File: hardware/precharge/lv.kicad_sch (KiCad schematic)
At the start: 44 parts

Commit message: Tweaks made during today's meeting
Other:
- note added: "Add a tiny delay from when SHUTDOWN changes, to prevent a glitch on FAULT due to unknown initial state of flip-flop."
- note removed: "Add a tiny delay from when SHUTDOWN changes, to prevent a glitch on FAULT."
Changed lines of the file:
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@@
     (effects (font (size 1.27 1.27)) (justify left bottom))
   )
-  (text "Add a tiny delay from\nwhen SHUTDOWN changes,\nto prevent a glitch on\nFAULT."
-    (at 155.575 123.825 0)
+  (text "Add a tiny delay from\nwhen SHUTDOWN changes,\nto prevent a glitch on\nFAULT due to unknown\ninitial state of\nflip-flop."
+    (at 131.445 133.35 0)
     (effects (font (size 1.27 1.27)) (justify left bottom))
   )

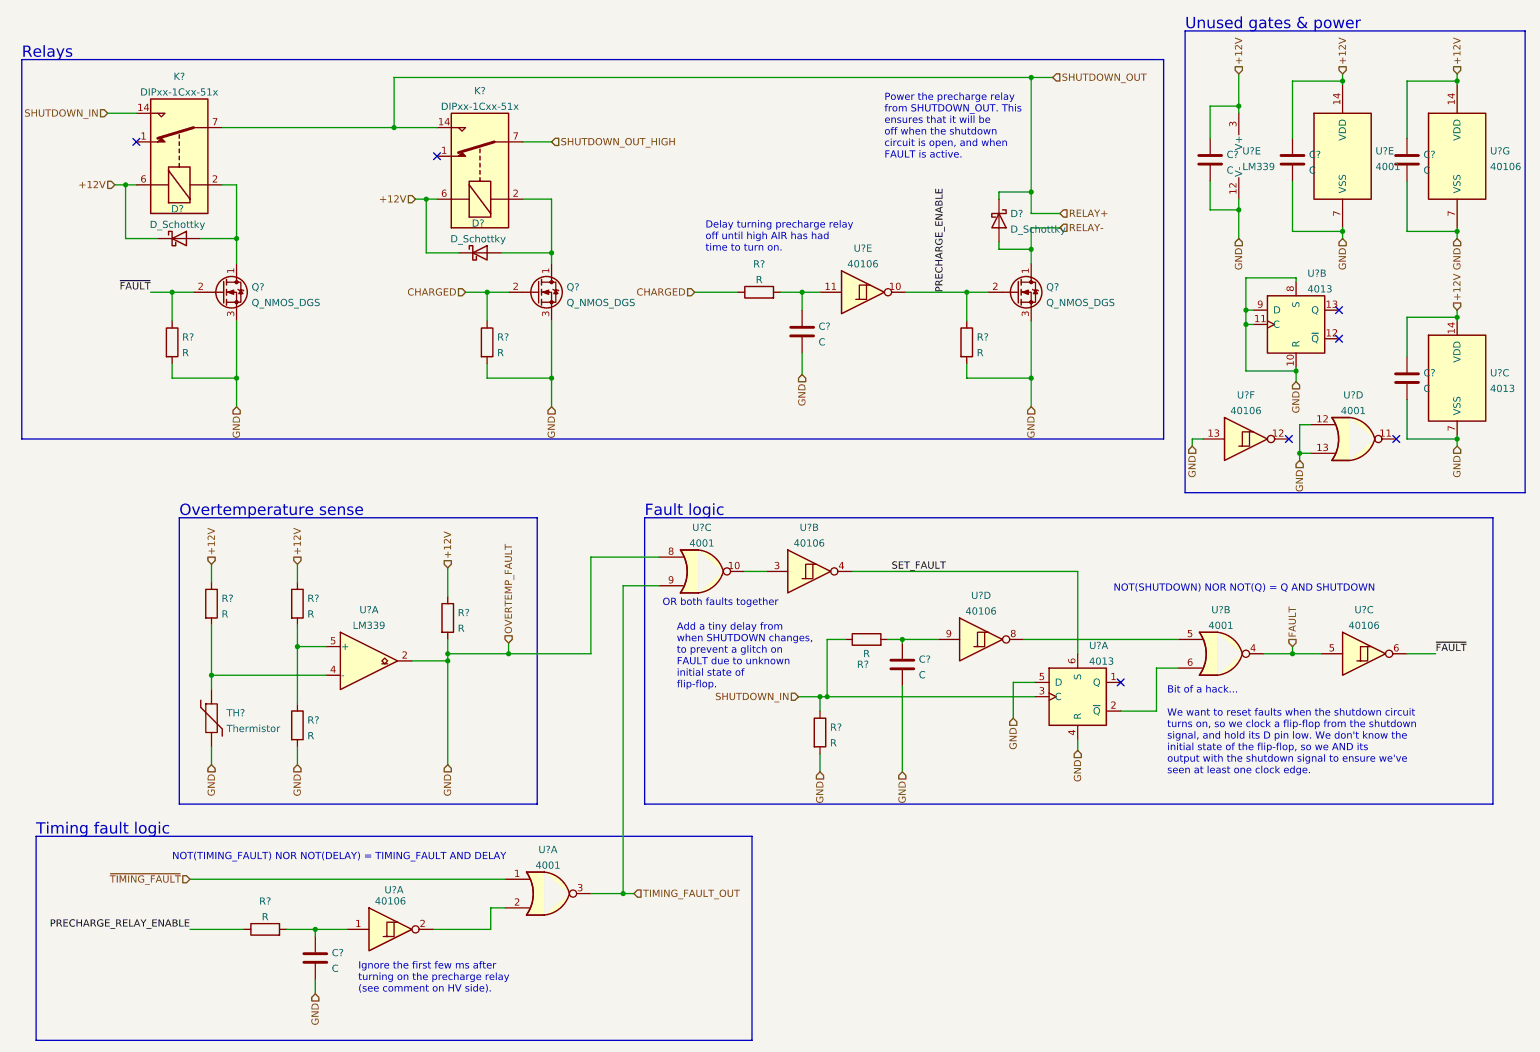
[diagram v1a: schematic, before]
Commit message: Updated quite a bit
- Added relay mechanical state detection

- Selected most component values for HV side

- Other miscellaneous changes
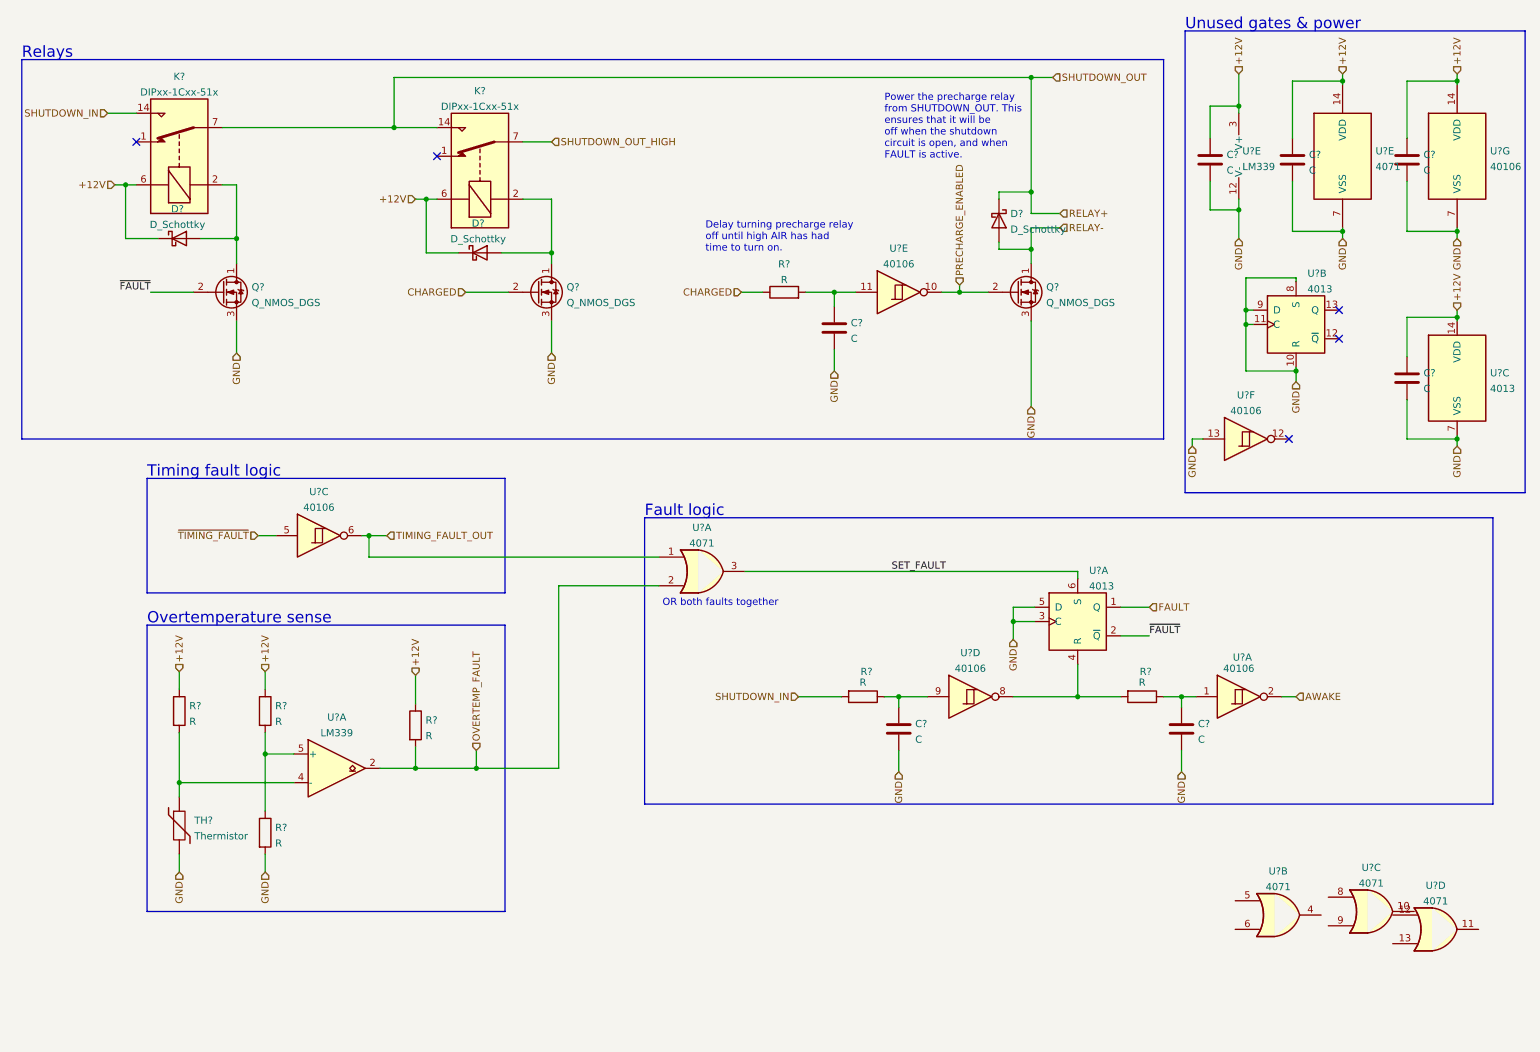
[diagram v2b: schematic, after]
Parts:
- removed C?: C, symbol Device:C
- removed R? (x5): R, symbol Device:R
- removed U? (x5): 4001, symbol 4xxx:4001
- removed U? (x2): 40106, symbol 4xxx:40106
- added C?: C, symbol Device:C
- added R?: R, symbol Device:R
- added U?: 40106, symbol 4xxx:40106
- added U? (x5): 4071, symbol 4xxx:4071
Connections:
- net +12V: now also U?.14 (VDD)
- net FAULT: now also U?.1 (Q); no longer U?.5
- net GND: now also C?.1, U?.3 (C), C?.1, U?.7 (VSS); no longer C?.2, R?.2, U?.2, U?.4 (R)
- net SET_FAULT: now also U?.3
- net SHUTDOWN_IN: now also R?.2; no longer R?.1, U?.3 (C)
- net TIMING_FAULT_OUT: now also U?.6, U?.1
- net ~{FAULT}: now also U?.2 (~{Q}); no longer U?.6
- net ~{TIMING_FAULT}: now also U?.5
- net at U?.1: now also C?.2, R?.1
- net AWAKE: now reaches U?.2
- net PRECHARGE_ENABLE renamed PRECHARGE_ENABLED
- new net: R?.2, U?.4 (R), U?.8
- new net: C?.2, R?.1, U?.9
- new net OVERTEMP_FAULT: R?.2, U?.2, U?.2
- no-connect marks 7 -> 5
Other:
- note removed: "Add a tiny delay from when SHUTDOWN changes, to prevent a glitch on FAULT due to unknown initial state of flip-flop."
- note removed: "Bit of a hack... We want to reset faults when the shutdown circuit turns on, so we clock a flip-flop from the shutdown signal, and hold its D pin low. We don't know the initial state of the flip-flop, so we AND its output with the shutdown signal to ensure we've seen at least one clock edge."
- note removed: "Ignore the first few ms after turning on the precharge relay (see comment on HV side)."
- note removed: "NOT(SHUTDOWN) NOR NOT(Q) = Q AND SHUTDOWN"
- note removed: "NOT(TIMING_FAULT) NOR NOT(DELAY) = TIMING_FAULT AND DELAY"
- moved on the sheet: C?, R?, TH?, U?A, U?C, U?E

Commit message: Added part numbers for most components, added LEDs, tweaked LV side.
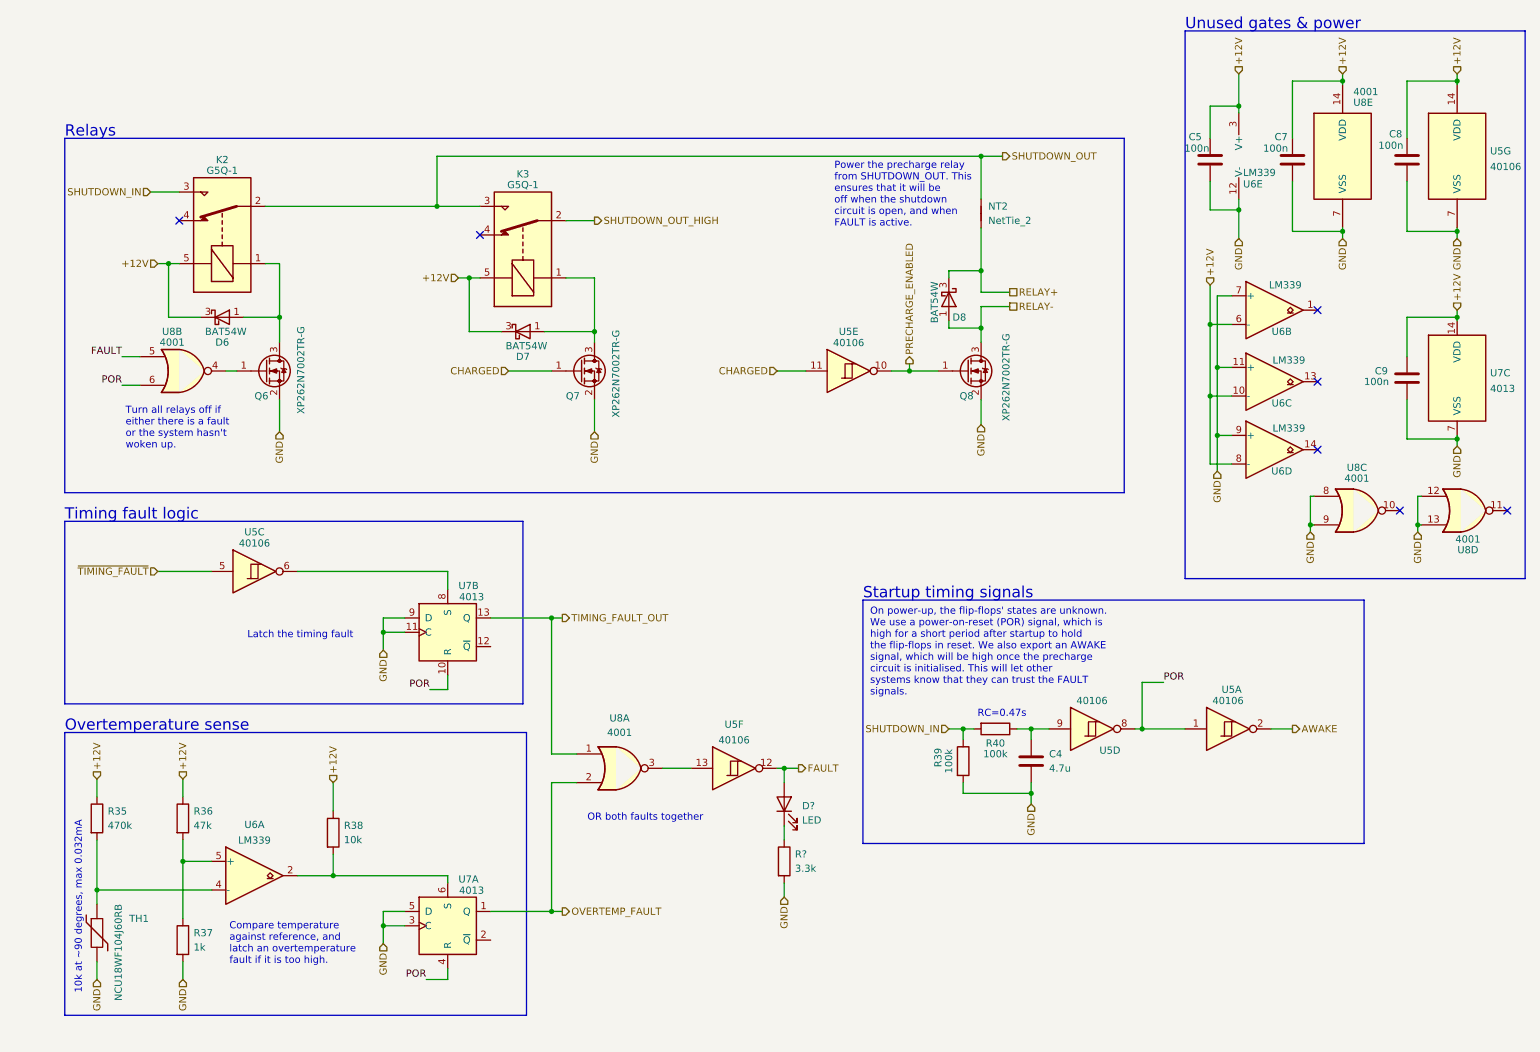
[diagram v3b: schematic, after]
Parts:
- removed C? (x2): C, symbol Device:C
- removed D? (x3): D_Schottky, symbol Device:D_Schottky
- removed K? (x2): DIPxx-1Cxx-51x, Relay_THT:Relay_StandexMeder_DIP_LowProfile, symbol Relay:DIPxx-1Cxx-51x
- removed Q? (x3): Q_NMOS_DGS, symbol Device:Q_NMOS_DGS
- removed R? (x2): R, symbol Device:R
- removed U? (x5): 4071, symbol 4xxx:4071
- added D6, D7, D8: BAT54W, Package_TO_SOT_SMD:SOT-323_SC-70, symbol Diode:BAT54W
- added D?: LED, symbol Device:LED
- added K2, K3: G5Q-1, Relay_THT:Relay_SPDT_Omron-G5Q-1, symbol Relay:G5Q-1
- added NT2: NetTie_2, symbol Device:NetTie_2
- added Q6, Q7, Q8: XP262N7002TR-G, symbol Device:Q_NMOS_GSD
- added R39: 100k, symbol Device:R
- added R?: 3.3k, symbol Device:R
- added unit 2 of U6
- added unit 4 of U6
- added unit 3 of U6
- added U8: 4001, symbol 4xxx:4001
- C4: renamed from C?; value C -> 4.7u
- C5, C7, C8, C9: renamed from C?; value C -> 100n
- R35: renamed from R?; value R -> 470k
- R36: renamed from R?; value R -> 47k
- R37: renamed from R?; value R -> 1k
- R38: renamed from R?; value R -> 10k
- R40: renamed from R?; value R -> 100k
- TH1: renamed from TH?; value Thermistor -> NCU18WF104J60RB
- gave numbers to parts that had none: 3
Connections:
- net +12V: now also D6.3 (K), D7.3 (K), K2.5, K3.5, U6.10 (-), U6.6 (-), U6.8 (-), U8.14 (VDD)
- net CHARGED: now also U5.11, Q7.1 (G)
- net FAULT: now also U5.12, D?.2 (A), U8.5; no longer U7.1 (Q)
- net GND: now also Q6.2 (S), Q7.2 (S), Q8.2 (S), R39.2, R?.2, U6.11 (+), U6.7 (+), U6.9 (+), U8.12, U8.13, U8.7 (VSS), U8.8, U8.9; no longer U5.13, U7.10 (R), U7.8 (S)
- net OVERTEMP_FAULT: now also U7.1 (Q), U8.2; no longer R38.2, U6.2
- net PRECHARGE_ENABLED: now also Q8.1 (G)
- net RELAY+: now also D8.3 (K), NT2.1
- net RELAY-: now also D8.1 (A), Q8.3 (D)
- net SHUTDOWN_IN: now also K2.3, R39.1
- net SHUTDOWN_OUT_HIGH: now also K3.2
- net TIMING_FAULT_OUT: now also U7.13 (Q), U8.1; no longer U5.6
- net POR: now reaches U5.8, U7.4 (R)
- net POR: now also U5.1, U7.10 (R), U8.6
- net SET_FAULT: no longer names the net of U7.6 (S)
- net SET_FAULT: now also R38.2, U6.2
- net ~{FAULT}: no longer names the net of U7.2 (~{Q})
- new net: Q6.1 (G), U8.4
- new net: D6.1 (A), K2.1, Q6.3 (D)
- new net: D?.1 (K), R?.1
- new net: D7.1 (A), K3.1, Q7.3 (D)
- new net: U5.13, U8.3
- new net: U5.6, U7.8 (S)
- new net SHUTDOWN_OUT: K2.2, K3.3, NT2.2
- no-connect marks 5 -> 7
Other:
- note added: "10k at ~90 degrees, max 0.032mA"
- note added: "Compare temperature against reference, and latch an overtemperature fault if it is too high."
- note added: "Latch the timing fault"
- note added: "On power-up, the flip-flops' states are unknown. We use a power-on-reset (POR) signal, which is high for a short period after startup to hold the flip-flops in reset. We also export an AWAKE signal, which will be high once the precharge circuit is initialised. This will let other systems know that they can trust the FAULT signals."
- note added: "RC=0.47s"
- note added: "Startup timing signals"
- note added: "Turn all relays off if either there is a fault or the system hasn't woken up."
- note removed: "Delay turning precharge relay off until high AIR has had time to turn on."
- note removed: "Fault logic"
- moved on the sheet: C4, R35, R36, R37, R38, R40, TH1, U5A, U5C, U5D, U5E, U5F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

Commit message: Tweaks, nearly done
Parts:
- gave numbers to parts that had none: 2
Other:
- moved on the sheet: U5F
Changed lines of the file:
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@@
     (stroke (width 0) (type default) (color 0 0 0 0))
   )
-  (wire (pts (xy 128.905 147.32) (xy 133.985 147.32))
+  (wire (pts (xy 128.905 147.32) (xy 130.175 147.32))
     (stroke (width 0) (type default) (color 0 0 0 0))
   )
@@
     (stroke (width 0) (type default) (color 0 0 0 0))
   )
-  (wire (pts (xy 149.225 147.32) (xy 150.495 147.32))
+  (wire (pts (xy 145.415 147.32) (xy 150.495 147.32))
     (stroke (width 0) (type default) (color 0 0 0 0))
   )
@@
   (symbol (lib_id "Device:R") (at 150.495 163.83 0) (unit 1)
     (in_bom yes) (on_board yes) (fields_autoplaced)
-    (property "Reference" "R?" (id 0) (at 152.4 162.5599 0)
+    (property "Reference" "R46" (id 0) (at 152.4 162.5599 0)
       (effects (font (size 1.27 1.27)) (justify left))
     )
@@
   (symbol (lib_id "Device:LED") (at 150.495 153.67 90) (unit 1)
     (in_bom yes) (on_board yes) (fields_autoplaced)
-    (property "Reference" "D?" (id 0) (at 153.67 153.9874 90)
+    (property "Reference" "D14" (id 0) (at 153.67 153.9874 90)
       (effects (font (size 1.27 1.27)) (justify right))
     )
@@
     (pin "2")
   )
-  (symbol (lib_id "4xxx:40106") (at 141.605 147.32 0) (unit 6)
+  (symbol (lib_id "4xxx:40106") (at 137.795 147.32 0) (unit 6)
     (in_bom yes) (on_board yes) (fields_autoplaced)
-    (property "Reference" "U5" (id 0) (at 141.605 139.5435 0))
-    (property "Value" "40106" (id 1) (at 141.605 142.3186 0))
-    (property "Footprint" "" (id 2) (at 141.605 147.32 0)
-      (effects (font (size 1.27 1.27)) hide)
-    )
-    (property "Datasheet" "https://assets.nexperia.com/documents/data-sheet/HEF40106B.pdf" (id 3) (at 141.605 147.32 0)
-      (effects (font (size 1.27 1.27)) hide)
-    )
+    (property "Reference" "U5" (id 0) (at 137.795 139.5435 0))
+    (property "Value" "40106" (id 1) (at 137.795 142.3186 0))
+    (property "Footprint" "" (id 2) (at 137.795 147.32 0)
+      (effects (font (size 1.27 1.27)) hide)
+    )
+    (property "Datasheet" "https://assets.nexperia.com/documents/data-sheet/HEF40106B.pdf" (id 3) (at 137.795 147.32 0)
+      (effects (font (size 1.27 1.27)) hide)
+    )

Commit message: Assigned some footprints, created footprint library
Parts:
- C4: footprint (none) -> Capacitor_SMD:C_0805_2012Metric
- C5, C7, C8, C9: footprint (none) -> Capacitor_SMD:C_0603_1608Metric
- D14: footprint (none) -> LED_SMD:LED_0603_1608Metric
- NT2: footprint (none) -> NetTie:NetTie-2_SMD_Pad0.5mm
- Q6, Q7, Q8: footprint (none) -> Package_TO_SOT_SMD:SOT-23
- R35, R36, R37, R38, R39, R40, R46, TH1: footprint (none) -> Resistor_SMD:R_0603_1608Metric
- U5, U6, U7, U8: footprint (none) -> Package_SO:SOIC-14_3.9x8.7mm_P1.27mm

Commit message: Preliminary PCB placement
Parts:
- removed C4: 4.7u, Capacitor_SMD:C_0805_2012Metric, symbol Device:C
- added C13: 4.7u, Capacitor_THT:CP_Radial_D5.0mm_P2.00mm, symbol Device:C_Polarized
- K2, K3: value G5Q-1 -> G5Q-1EU DC12
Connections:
- net GND: now also C13.2
- net at R40.1, U5.9: now also C13.1
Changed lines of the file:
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@@
     (in_bom yes) (on_board yes)
     (property "Reference" "K2" (id 0) (at 50.8 39.37 90))
-    (property "Value" "G5Q-1" (id 1) (at 50.8 41.275 90))
+    (property "Value" "G5Q-1EU DC12" (id 1) (at 50.8 41.275 90))
     (property "Footprint" "Relay_THT:Relay_SPDT_Omron-G5Q-1" (id 2) (at 52.07 41.275 0)
       (effects (font (size 1.27 1.27)) (justify left) hide)
@@
     (pin "9")
   )
-  (symbol (lib_id "Device:C") (at 194.31 146.05 180) (unit 1)
-    (in_bom yes) (on_board yes)
-    (property "Reference" "C4" (id 0) (at 197.485 144.78 0)
-      (effects (font (size 1.27 1.27)) (justify right))
-    )
-    (property "Value" "4.7u" (id 1) (at 197.485 147.32 0)
-      (effects (font (size 1.27 1.27)) (justify right))
-    )
-    (property "Footprint" "Capacitor_SMD:C_0805_2012Metric" (id 2) (at 193.3448 142.24 0)
-      (effects (font (size 1.27 1.27)) hide)
-    )
-    (property "Datasheet" "~" (id 3) (at 194.31 146.05 0)
-      (effects (font (size 1.27 1.27)) hide)
-    )
-    (pin "1")
-    (pin "2")
-  )
   (symbol (lib_id "Comparator:LM339") (at 233.68 38.735 0) (unit 5)
     (in_bom yes) (on_board yes)
@@
     (in_bom yes) (on_board yes)
     (property "Reference" "K3" (id 0) (at 104.14 41.91 90))
-    (property "Value" "G5Q-1" (id 1) (at 104.14 43.815 90))
+    (property "Value" "G5Q-1EU DC12" (id 1) (at 104.14 43.815 90))
     (property "Footprint" "Relay_THT:Relay_SPDT_Omron-G5Q-1" (id 2) (at 105.41 43.815 0)
       (effects (font (size 1.27 1.27)) (justify left) hide)
@@
     (pin "6")
   )
+  (symbol (lib_id "Device:C_Polarized") (at 194.31 146.05 0) (unit 1)
+    (in_bom yes) (on_board yes) (fields_autoplaced)
+    (property "Reference" "C13" (id 0) (at 198.12 143.8909 0)
+      (effects (font (size 1.27 1.27)) (justify left))
+    )
+    (property "Value" "4.7u" (id 1) (at 198.12 146.4309 0)
+      (effects (font (size 1.27 1.27)) (justify left))
+    )
+    (property "Footprint" "Capacitor_THT:CP_Radial_D5.0mm_P2.00mm" (id 2) (at 195.2752 149.86 0)
+      (effects (font (size 1.27 1.27)) hide)
+    )
+    (property "Datasheet" "~" (id 3) (at 194.31 146.05 0)
+      (effects (font (size 1.27 1.27)) hide)
+    )
+    (pin "1")
+    (pin "2")
+  )
   (symbol (lib_id "Device:C") (at 260.985 39.37 0) (unit 1)
